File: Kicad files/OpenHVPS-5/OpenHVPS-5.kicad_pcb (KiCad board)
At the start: 2 copper layers, 40.6 x 20.8 mm, 82 parts, among them J1 Conn_01x03_Male, Q1 FQT7N10, Q2 BC846A, Q3 MMBT3906, Q4 MMBT3906, U1 MAX6008AEUR+T, U2 74HC14, U3 MAX4162, U4 CD14538BM

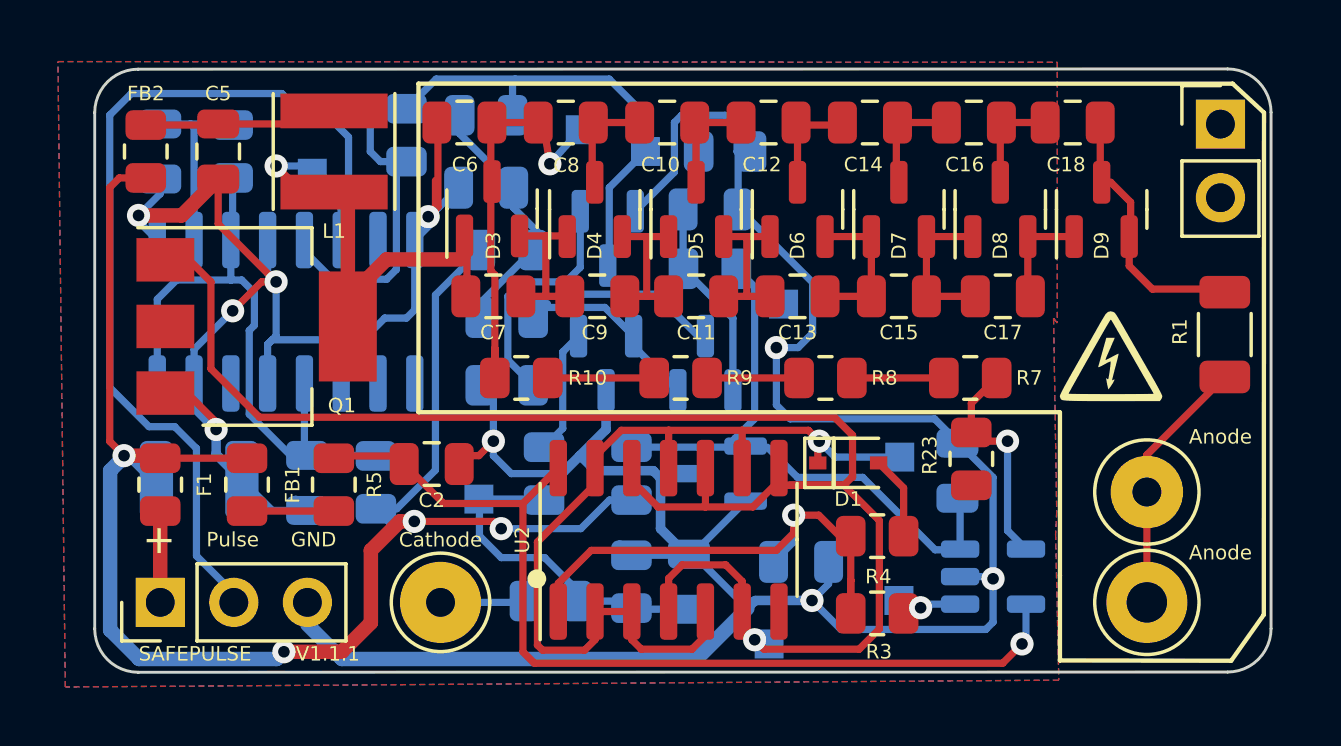
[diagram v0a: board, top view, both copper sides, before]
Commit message: Updated RC network around opamp and text changes.
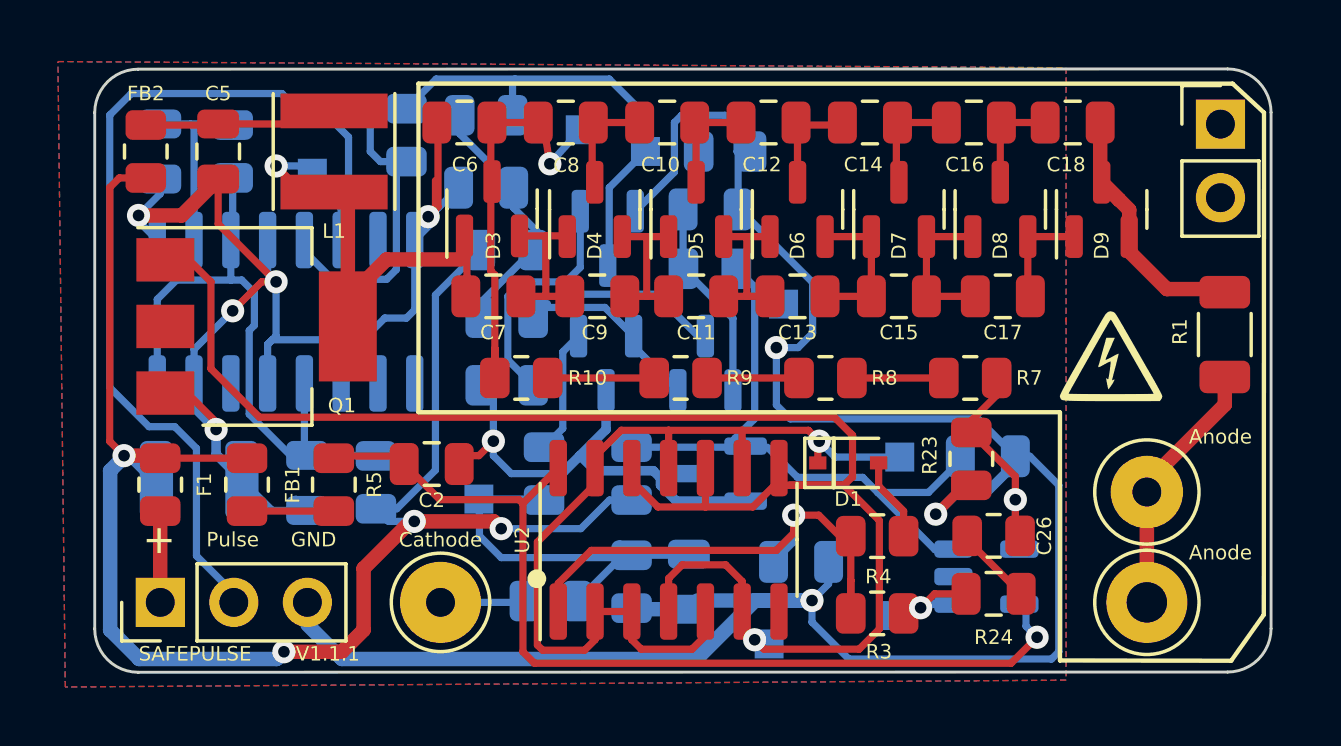
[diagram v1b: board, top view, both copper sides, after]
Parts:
- added C26: 100pF, Capacitor_SMD:C_0805_2012Metric, F.Cu at (157.3, 75.3)
- added R24: 22M, Resistor_SMD:R_0805_2012Metric, F.Cu at (157.3, 73.3)
- moved C25 1.16 mm to (157.1, 70.5), turned to 0 degrees
- moved TP2 0.57 mm to (153.8, 76.0)
- moved U3 0.23 mm to (157.0, 74.7)
- turned R22 to -90 degrees
- turned C22 to -90 degrees
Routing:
- net GND: track 139.1 -> 149.8 mm
- net Net-(R3-Pad2): track 1.41 -> 5.61 mm
- net Net-(C22-Pad1): track 11.8 -> 14.8 mm
- net Net-(R24-Pad1): track 0.00 -> 2.77 mm
- net +2V5: track 23.8 -> 25.4 mm
- net Net-(R23-Pad1): track 7.61 -> 8.76 mm

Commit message: Updated  with TP and some other small changes.
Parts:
- moved TP1 0.25 mm to (150.3, 65.3)
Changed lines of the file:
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@@
   )
   (footprint "TestPoint:TestPoint_Pad_1.0x1.0mm" (layer "B.Cu")
-    (at 150.02 65.27 180)
+    (at 150.27 65.27 180)
     (descr "SMD rectangular pad as test Point, square 1.0mm side length")
     (tags "test point SMD pad rectangle square")
@@
   (segment (start 142.433 71.12) (end 140.62 71.12) (width 0.25) (layer "B.Cu") (net 3))
   (segment (start 127.75 62.208) (end 127.75 62.41) (width 0.25) (layer "B.Cu") (net 3))
+  (segment (start 148.45 62) (end 148.5 62) (width 0.25) (layer "B.Cu") (net 3))
   (segment (start 152.27 77.52) (end 159.27 77.52) (width 0.25) (layer "B.Cu") (net 3))
-  (segment (start 148.45 62) (end 148.5 62) (width 0.25) (layer "B.Cu") (net 3))
   (segment (start 134.1026 66.5) (end 134.747 67.1444) (width 0.25) (layer "B.Cu") (net 3))
   (segment (start 127.75 62.41) (end 128.397 63.057) (width 0.25) (layer "B.Cu") (net 3))
   (segment (start 139.428 68.072) (end 139.5495 68.072) (width 0.25) (layer "B.Cu") (net 3))
+  (segment (start 151.27 64.77) (end 151.27 66.02) (width 0.25) (layer "B.Cu") (net 3))
   (segment (start 137.832 62.332) (end 137.832 62.5121) (width 0.25) (layer "B.Cu") (net 3))
   (segment (start 149.77 68.75) (end 150.25 69.23) (width 0.25) (layer "B.Cu") (net 3))
@@
   (segment (start 137.75 62.25) (end 137.8 62.25) (width 0.25) (layer "B.Cu") (net 3))
   (segment (start 151 76.25) (end 152.27 77.52) (width 0.25) (layer "B.Cu") (net 3))
+  (segment (start 150.52 66.77) (end 149.77 66.77) (width 0.25) (layer "B.Cu") (net 3))
   (segment (start 148.4125 59.1625) (end 148.4125 60) (width 0.25) (layer "B.Cu") (net 3))
   (segment (start 149.04 75.5) (end 151 75.5) (width 0.5) (layer "B.Cu") (net 3))
@@
   (segment (start 148.336 72.0325) (end 148.37 72.0665) (width 0.25) (layer "B.Cu") (net 3))
   (segment (start 158.02 70.77) (end 158.02 70.52) (width 0.3302) (layer "B.Cu") (net 3))
-  (segment (start 151.02 64.52) (end 151.02 66.27) (width 0.25) (layer "B.Cu") (net 3))
   (segment (start 132.5 64.5) (end 132.5 66.3677) (width 0.25) (layer "B.Cu") (net 3))
   (segment (start 151 75.5) (end 151 76.25) (width 0.25) (layer "B.Cu") (net 3))
@@
   (segment (start 128.5 61.458) (end 128.5 60.95) (width 0.25) (layer "B.Cu") (net 3))
   (segment (start 142.993864 70.493864) (end 143.52 71.02) (width 0.3302) (layer "B.Cu") (net 3))
-  (segment (start 150.52 66.77) (end 149.77 66.77) (width 0.25) (layer "B.Cu") (net 3))
   (segment (start 159.27 77.52) (end 159.52 77.27) (width 0.25) (layer "B.Cu") (net 3))
   (segment (start 149.77 66.77) (end 149.77 68.75) (width 0.25) (layer "B.Cu") (net 3))
@@
   (segment (start 143.891 69.596728) (end 142.993864 70.493864) (width 0.3302) (layer "B.Cu") (net 3))
   (segment (start 140.62 71.12) (end 140 70.5) (width 0.25) (layer "B.Cu") (net 3))
+  (segment (start 151.27 66.02) (end 150.52 66.77) (width 0.25) (layer "B.Cu") (net 3))
   (segment (start 132.207 66.6607) (end 132.3677 66.5) (width 0.25) (layer "B.Cu") (net 3))
   (segment (start 143.891 68.2475) (end 143.891 69.596728) (width 0.3302) (layer "B.Cu") (net 3))
@@
   (segment (start 133.4615 72.5) (end 133.57 72.3915) (width 0.25) (layer "B.Cu") (net 3))
   (segment (start 132.5 64.5) (end 132.207 64.207) (width 0.25) (layer "B.Cu") (net 3))
-  (segment (start 148.5 62) (end 151.02 64.52) (width 0.25) (layer "B.Cu") (net 3))
   (segment (start 158.52 70.52) (end 158.02 70.52) (width 0.25) (layer "B.Cu") (net 3))
   (segment (start 137 65.75) (end 137.287 65.463) (width 0.25) (layer "B.Cu") (net 3))
@@
   (segment (start 157.02 71.77) (end 158.02 70.77) (width 0.3302) (layer "B.Cu") (net 3))
   (segment (start 151.5 74.096) (end 151.572 74.168) (width 0.25) (layer "B.Cu") (net 3))
-  (segment (start 151.02 66.27) (end 150.52 66.77) (width 0.25) (layer "B.Cu") (net 3))
   (segment (start 130.429 70.4525) (end 131.318 71.3415) (width 0.3302) (layer "B.Cu") (net 3))
   (segment (start 129.667 66.833) (end 129.667 68.007) (width 0.25) (layer "B.Cu") (net 3))
   (segment (start 140 70) (end 140 68.5225) (width 0.25) (layer "B.Cu") (net 3))
   (segment (start 148.45 62) (end 148.45 60.0375) (width 0.25) (layer "B.Cu") (net 3))
+  (segment (start 148.5 62) (end 151.27 64.77) (width 0.25) (layer "B.Cu") (net 3))
   (segment (start 146.32 72.07) (end 148.7075 72.07) (width 0.3302) (layer "B.Cu") (net 3))
   (segment (start 134.05 59.05) (end 134.5 58.6) (width 0.25) (layer "F.Cu") (net 4))

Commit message: Changed layout
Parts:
- C19, C3, D2, R11, R13, R17, R18, R6, U4: moved to F.Cu
- C2, C26, D1, FB1, R23, R24, R3, R4, R5, U2: moved to B.Cu
- moved D2 28.7 mm to (157.5, 75.3), turned to 90 degrees
- moved C3 22.7 mm to (144.3, 76.3), turned to 0 degrees
- moved TP4 21.0 mm to (130.5, 68.0)
- moved TP3 20.8 mm to (133.3, 71.0)
- moved U4 20.1 mm to (151.3, 73.5), turned to 90 degrees
- moved R6 19.0 mm to (145.0, 72.8), turned to -90 degrees
- moved U3 18.2 mm to (143.0, 63.0)
- moved R17 18.0 mm to (157.5, 71.4), turned to -90 degrees
- moved D1 17.9 mm to (134.5, 68.2), turned to -90 degrees
- moved R4 17.5 mm to (136.5, 68.2), turned to -90 degrees
- moved R11 16.9 mm to (141.5, 75.8)
- moved C25 16.8 mm to (144.8, 59.0), turned to 90 degrees
- moved C23 16.4 mm to (149.3, 76.3), turned to 0 degrees
- moved C26 16.3 mm to (146.5, 63.0), turned to 90 degrees
- moved U2 15.2 mm to (135.3, 62.7)
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- renumbered G2 to G3
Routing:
- net Net-(Q1-Pad1): track 59.1 -> 28.5 mm
- net +3V3: track 58.4 -> 36.7 mm, vias 4 -> 3
- net Net-(C19-Pad1): track 9.01 -> 23.3 mm
- net Net-(C1-Pad1): track 18.6 -> 6.52 mm, vias 1 -> 0
- net Net-(D2-Pad2): track 31.6 -> 43.1 mm
- net Net-(D2-Pad1): track 11.1 -> 19.9 mm
- net Net-(Q2-Pad1): track 15.0 -> 6.19 mm
- net Net-(R23-Pad1): track 8.76 -> 17.4 mm
- net GND: track 150.0 -> 158.3 mm, vias 9 -> 11
- net Net-(C2-Pad1): track 34.0 -> 26.7 mm, vias 1 -> 0
- net Net-(C26-Pad1): track 5.61 -> 10.7 mm, vias 1 -> 0
- net Net-(D1-Pad1): track 31.1 -> 26.7 mm, vias 1 -> 0
- net Net-(Q2-Pad3): track 16.2 -> 20.4 mm, vias 0 -> 1
- net Net-(C24-Pad1): track 9.50 -> 12.6 mm
- net Net-(Q4-Pad1): track 4.33 -> 2.06 mm
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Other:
- board text added: "SAFEPULSE V1.1.2"
- board text removed: "SAFEPULSE V1.1.1"

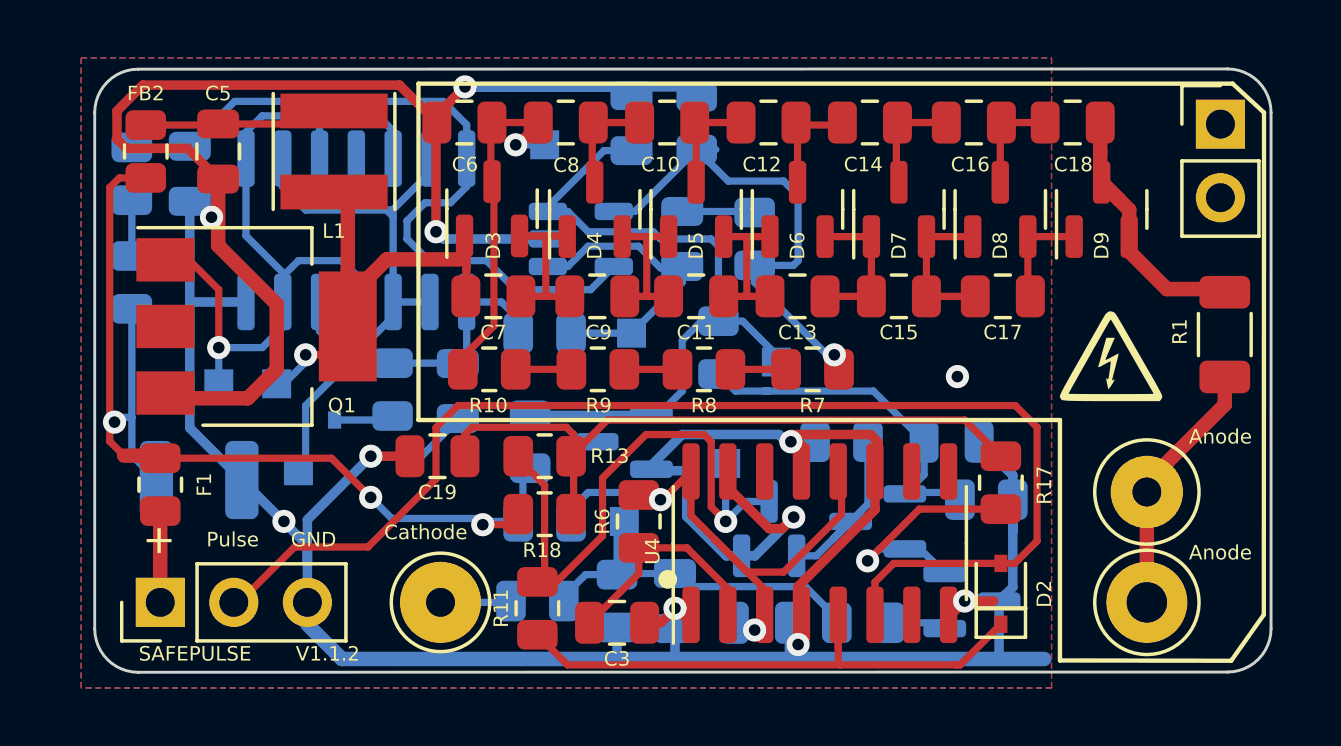
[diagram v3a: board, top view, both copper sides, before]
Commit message: Update text from SafePulse V1.1.2
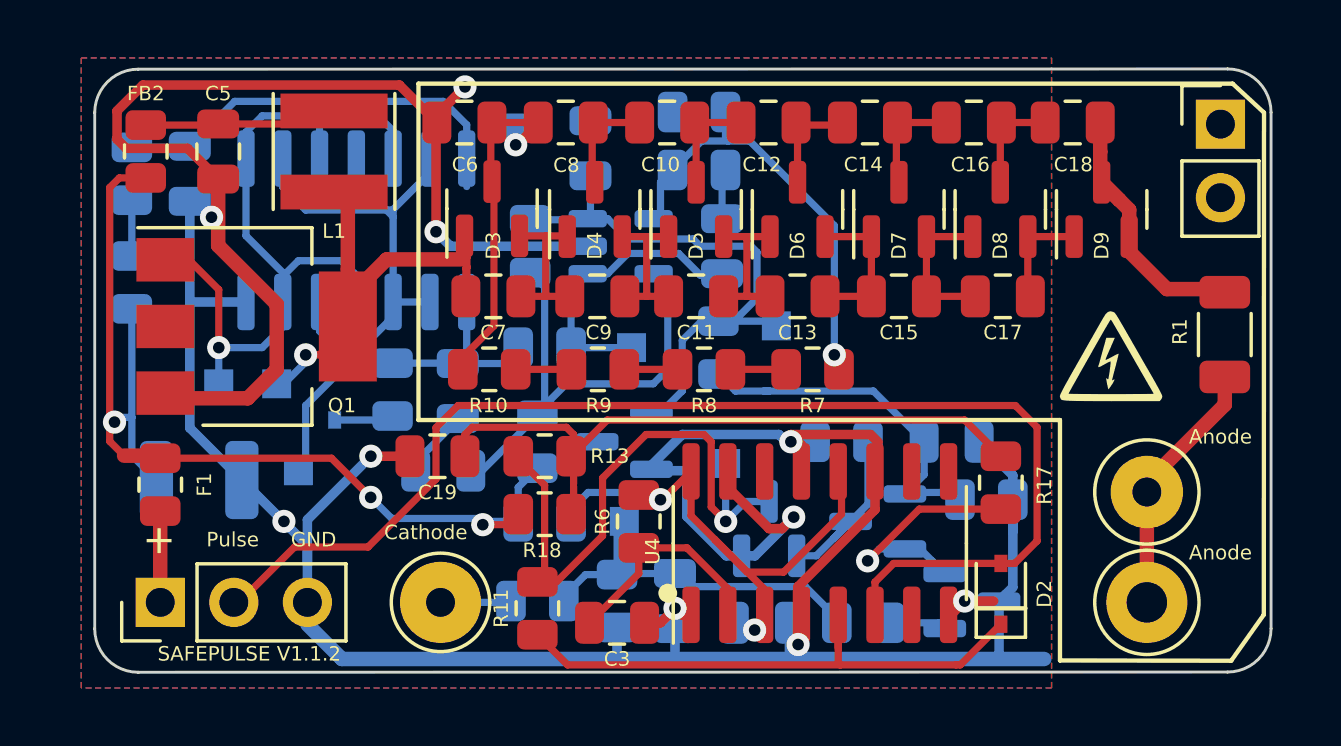
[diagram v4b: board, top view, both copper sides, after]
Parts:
- added C27: 1uF, Capacitor_SMD:C_0805_2012Metric, B.Cu at (138.3, 71.0)
- added R25: 100, Resistor_SMD:R_0805_2012Metric, B.Cu at (141.5, 70.0)
- moved R20 6.75 mm to (141.3, 63.3)
- moved R24 3.06 mm to (147.1, 60.6), turned to 180 degrees
- moved C25 1.66 mm to (143.4, 59.9)
- moved C26 1.40 mm to (147.9, 63.3)
- moved U3 1.40 mm to (144.4, 63.3)
- moved TP1 1.25 mm to (149.8, 66.0)
- moved TP6 1.02 mm to (140.9, 59.2)
- moved R3 0.50 mm to (141.8, 66.8)
- moved TP2 0.50 mm to (144.8, 66.8)
- moved R23 0.39 mm to (147.1, 58.6), turned to 180 degrees
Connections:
- R20 pad 1: +3V3 -> Net-(U3-Pad5)
- U3 pad 5: Net-(C2-Pad1) -> Net-(U3-Pad5)
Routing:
- net Net-(U3-Pad5): track 0.00 -> 17.2 mm
- net GND: track 158.3 -> 145.3 mm, vias 11 -> 10
- net Net-(C2-Pad1): track 26.7 -> 15.3 mm
- net +2V5: track 25.0 -> 20.6 mm
- net Net-(R23-Pad1): track 17.4 -> 15.6 mm
- net Net-(C6-Pad2): track 13.6 -> 12.6 mm
- net Net-(C26-Pad1): track 10.7 -> 9.77 mm
- net +3V3: track 36.7 -> 37.5 mm
- net Net-(C26-Pad2): track 2.52 -> 1.73 mm

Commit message: Chnaged R4 and C1 label placement
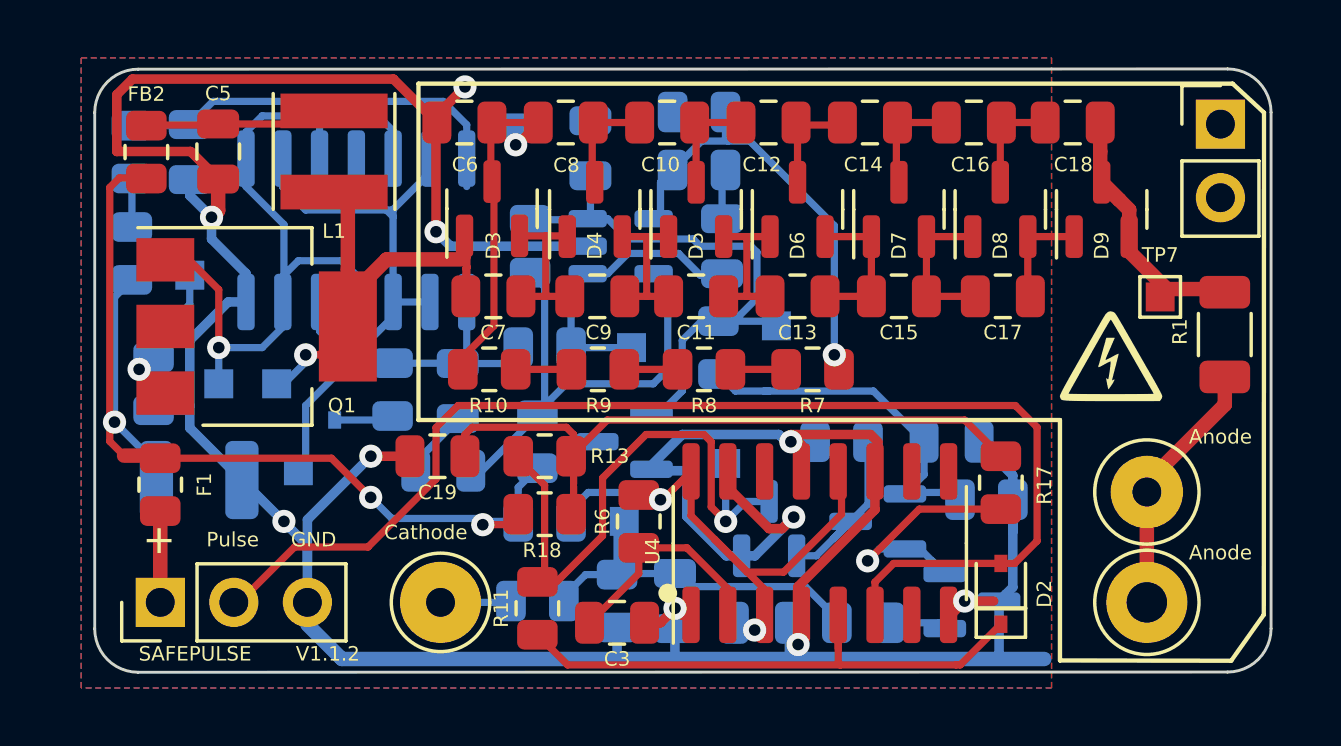
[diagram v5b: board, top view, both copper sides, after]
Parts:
- added R26: 0.1E, Resistor_SMD:R_0805_2012Metric, B.Cu at (128.3, 68.0)
- added TP10: TestPoint, TestPoint:TestPoint_Pad_1.0x1.0mm, B.Cu at (129.5, 64.3)
- added TP7: TestPoint, TestPoint:TestPoint_Pad_1.0x1.0mm, F.Cu at (163.0, 65.0)
- C19: value 0.1uF -> 10uF
- C2, C23, C27, C5: value 1uF -> 10uF
- C22: value 360pF -> 390pF
- C24: value 1nF -> 10nF
- C4: value 10uF -> 100uF
- moved FB1 1.00 mm to (127.5, 63.5)
- moved C2 0.75 mm to (129.5, 60.0)
- moved R5 0.75 mm to (127.5, 60.0)
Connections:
- Q1 pad 3: GND -> Net-(Q1-Pad3)
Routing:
- net GND: track 145.3 -> 136.0 mm
- net Net-(Q1-Pad3): track 0.00 -> 5.96 mm, vias 0 -> 1
- net +3V3: track 37.5 -> 38.6 mm

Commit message: Updated ground plane changed, capacitor to 47uF
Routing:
- net +2V5: track 20.6 -> 19.4 mm
- net GND: track 136.0 -> 136.4 mm, vias 10 -> 11
